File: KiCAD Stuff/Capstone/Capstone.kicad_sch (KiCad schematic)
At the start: 29 parts, among them J1 Conn_01x02_Socket, U1 TPS61094, U2 TC1044, U3 INA818, U4 TLV9101

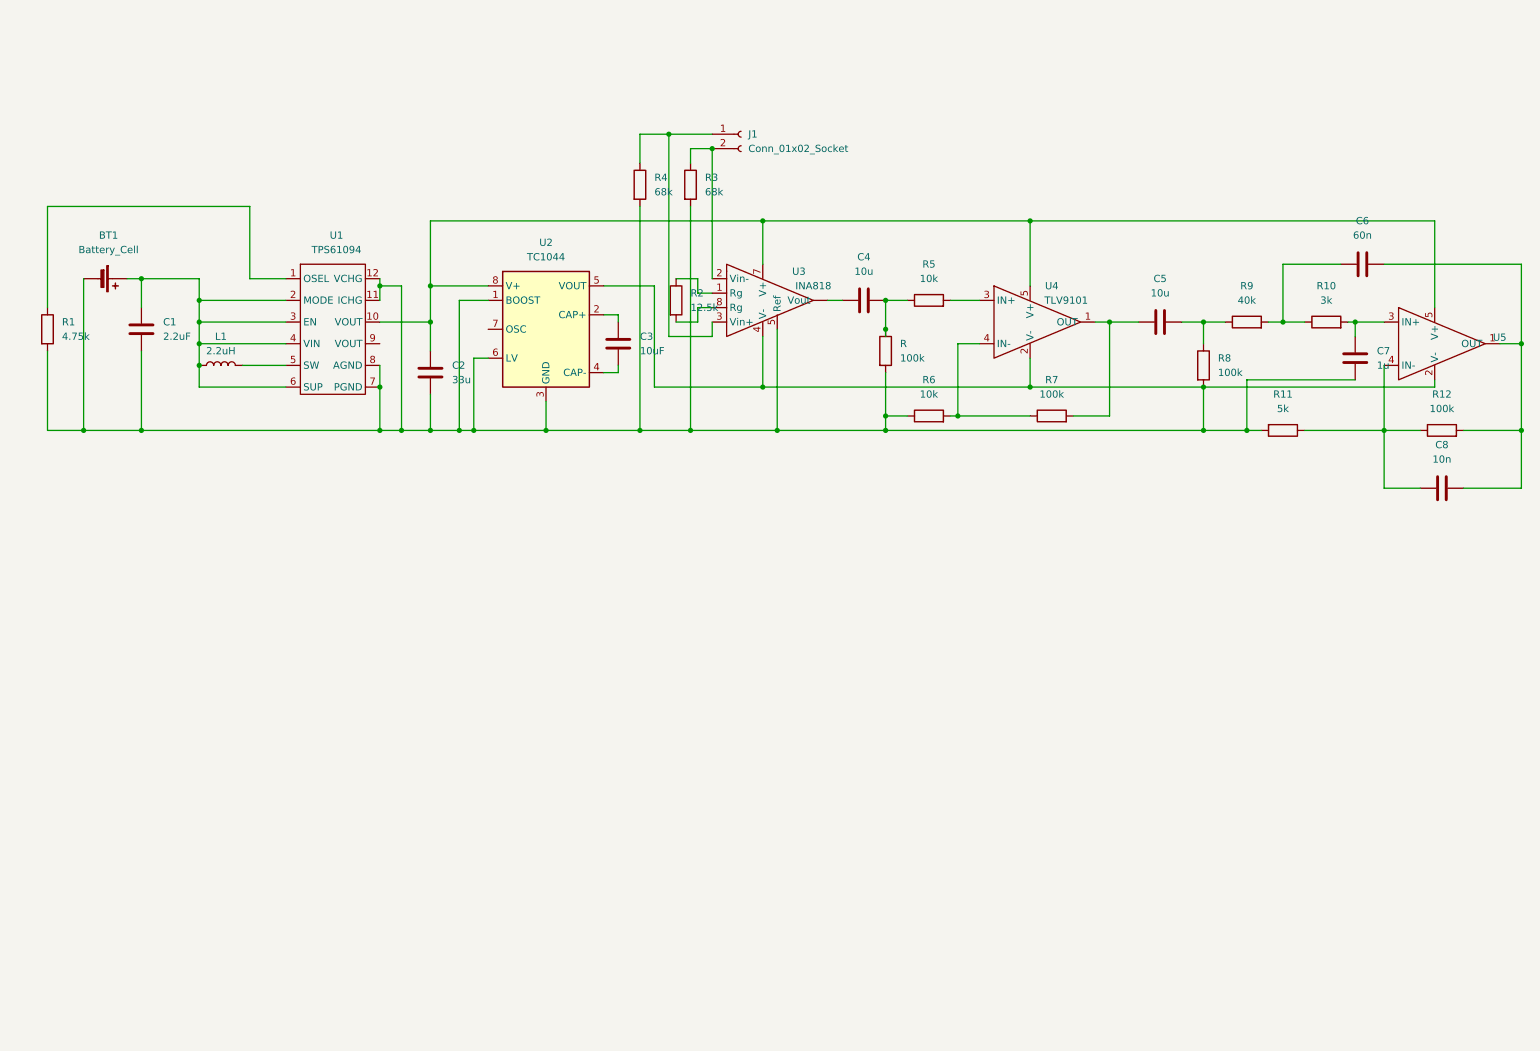
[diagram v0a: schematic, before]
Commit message: Clarified schematic topology
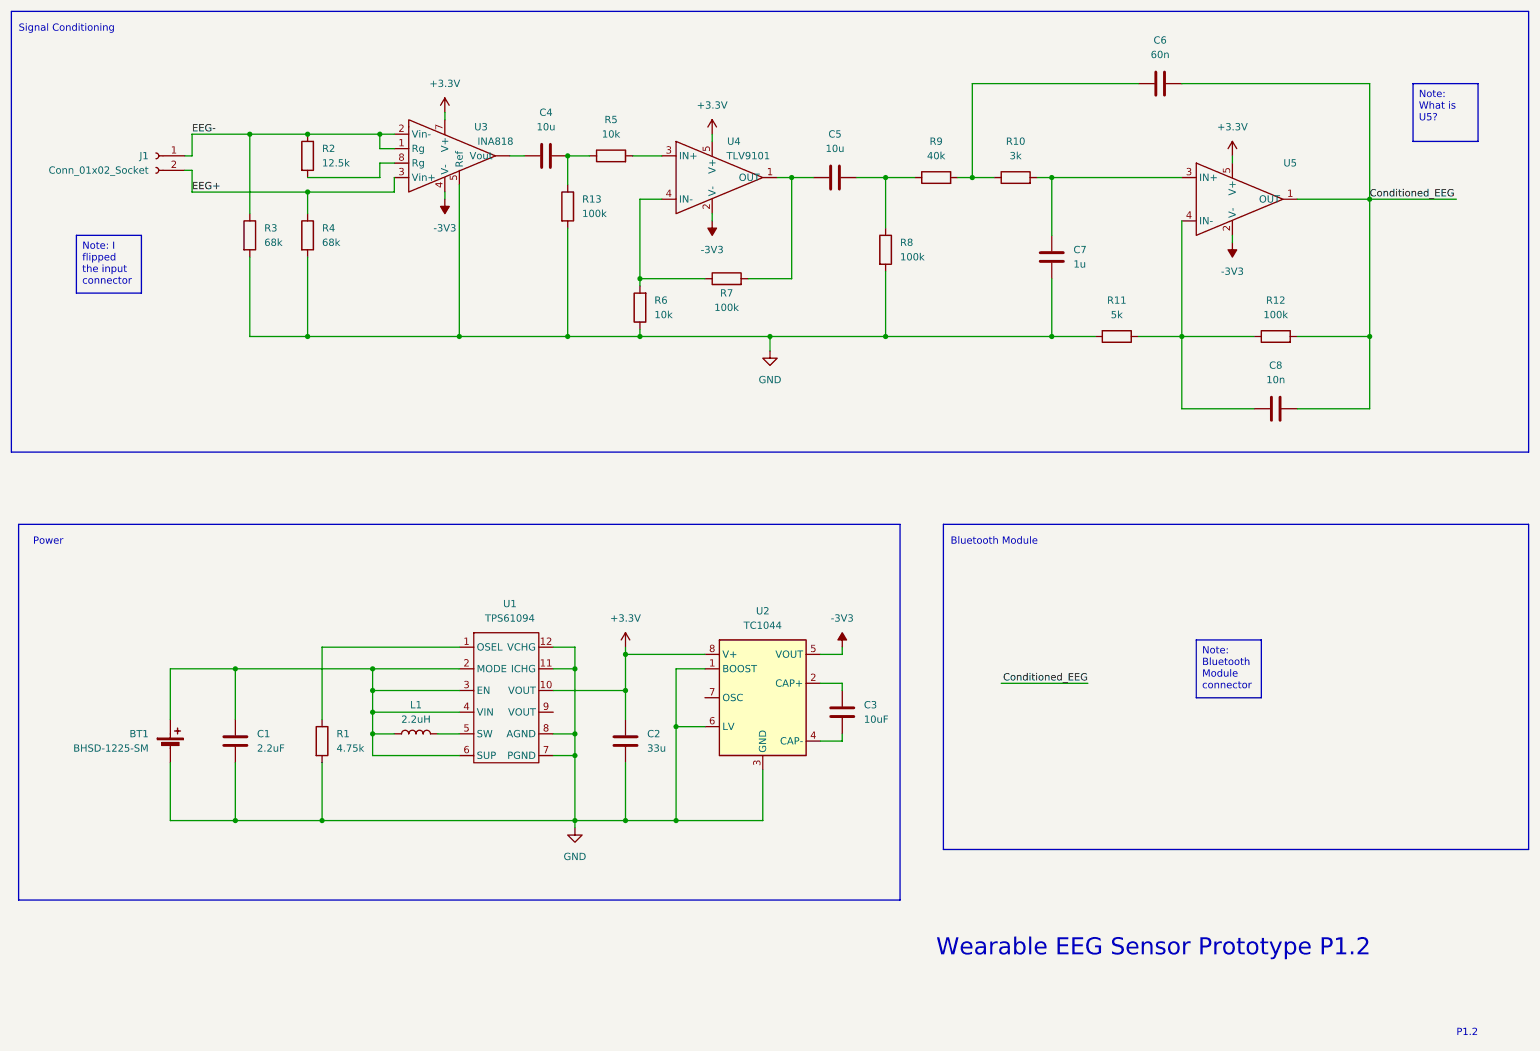
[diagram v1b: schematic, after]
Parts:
- BT1: value Battery_Cell -> BHSD-1225-SM
- renumbered R to R13
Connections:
- net GND: now reaches BT1.2 (-), C1.2, C2.2, C7.1, R1.2, R11.2, R13.2, R3.2, R4.2, R6.1, R8.2, U1.11 (ICHG), U1.12 (VCHG), U1.7 (PGND), U1.8 (AGND), U2.1 (BOOST), U2.3 (GND), U2.6 (LV), U3.5 (Ref)
- net GND: no longer U2.5 (VOUT), U3.4 (V-), U4.2 (V-), U5.2 (V-)
- net EEG-: now reaches R3.1, U3.2 (Vin-)
- net EEG-: now also J1.1 (Pin_1), R2.1, U3.1 (Rg); no longer J1.2 (Pin_2)
- net Conditioned_EEG: now reaches C6.1, C8.1, R12.2, U5.1 (OUT)
- net +3.3V: now reaches C2.1, U1.10 (VOUT), U2.8 (V+), U3.7 (V+), U4.5 (V+), U5.5 (V+)
- net EEG+: now reaches R4.1, U3.3 (Vin+)
- net EEG+: now also J1.2 (Pin_2); no longer J1.1 (Pin_1)
- new net -3V3: U2.5 (VOUT), U3.4 (V-), U4.2 (V-), U5.2 (V-)
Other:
- note added: "Bluetooth Module"
- note added: "P1.2"
- note added: "Power"
- note added: "Signal Conditioning"
- note added: "Wearable EEG Sensor Prototype P1.2"
- moved on the sheet: BT1, C1, C2, C3, C4, C5, C6, C7, C8, L1, R1, R10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

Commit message: Added some footprints to schematic
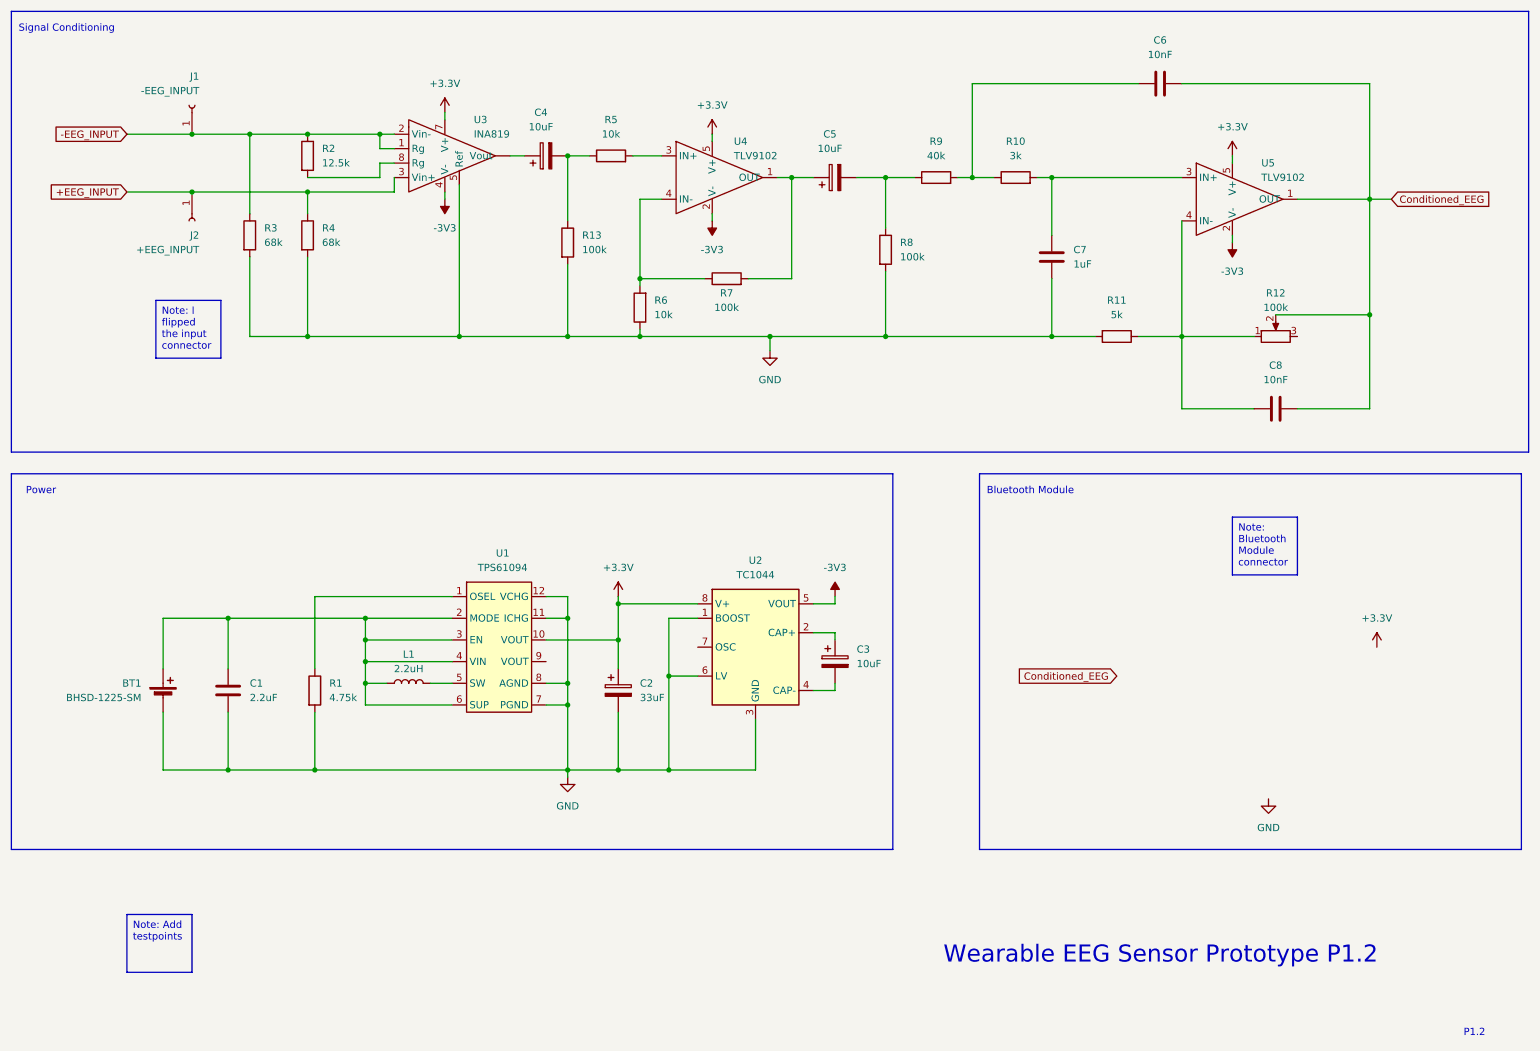
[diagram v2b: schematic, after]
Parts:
- removed J1: Conn_01x02_Socket, symbol Connector:Conn_01x02_Socket
- added J1: -EEG_INPUT, symbol Connector:Conn_01x01_Socket
- added J2: +EEG_INPUT, symbol Connector:Conn_01x01_Socket
- C1: footprint (none) -> Capacitor_THT:C_Rect_L7.0mm_W4.5mm_P5.00mm
- C2: value 33u -> 33uF; footprint (none) -> Capacitor_THT:CP_Radial_D8.0mm_P5.00mm; symbol Device:C -> Device:C_Polarized
- C3: footprint (none) -> Capacitor_THT:CP_Radial_D5.0mm_P2.50mm; symbol Device:C -> Device:C_Polarized
- C4, C5: value 10u -> 10uF; footprint (none) -> Capacitor_THT:CP_Radial_D5.0mm_P2.50mm; symbol Device:C -> Device:C_Polarized
- C6: value 60n -> 10nF; footprint (none) -> Capacitor_THT:C_Rect_L7.0mm_W2.5mm_P5.00mm
- C7: value 1u -> 1uF; footprint (none) -> Capacitor_THT:C_Rect_L7.0mm_W4.5mm_P5.00mm
- C8: value 10n -> 10nF; footprint (none) -> Capacitor_THT:C_Rect_L7.0mm_W2.5mm_P5.00mm
- R1, R10, R11, R13, R2, R3, R4, R5, R6, R7, R8, R9: footprint (none) -> Resistor_THT:R_Axial_DIN0207_L6.3mm_D2.5mm_P10.16mm_Horizontal
- R12: footprint (none) -> Resistor_THT:R_Axial_DIN0207_L6.3mm_D2.5mm_P10.16mm_Horizontal; symbol Device:R -> Device:R_Potentiometer
- U3: value INA818 -> INA819
- U4: value TLV9101 -> TLV9102
- U5: value ~ -> TLV9102
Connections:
- net EEG+ renamed +EEG_INPUT
- net +EEG_INPUT: now also J2.1 (Pin_1)
- net EEG- renamed -EEG_INPUT
- net -EEG_INPUT: now also J1.1 (Pin_1)
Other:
- moved on the sheet: BT1, C1, L1, R1, R13, U2
